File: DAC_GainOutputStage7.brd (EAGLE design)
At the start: 110 x 105.3 mm, 70 parts, among them J1 1935190, J3 SJ-63033A, U1 LM317MQDCYR, U2 LM317MQDCYR

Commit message: Adding trimmer resistor for CCS
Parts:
- removed R10, R16: 48.7, Dual Mono Amp Library:0207/10
- added TP1, TP2: TPB2,54, Dual Mono Amp Library:B2,54
- added VR1, VR2: PVG5A101C03R00, Dual Mono Amp Library:PVG5A101C03R00
- moved R3O 16.0 mm to (2.03, 58.9), turned to 90 degrees
- moved R3O1 16.0 mm to (108.0, 58.9), turned to 90 degrees
- moved U1 11.0 mm to (15.5, 48.5), turned to 270 degrees
- moved U2 11.0 mm to (94.5, 48.5)
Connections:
- net AGND: now also VR1.3, VR2.3; no longer R10.1, R16.1
- net N$23: now also TP1.TP
- net N$29: now also TP2.TP
- net N$37: now also VR2.1, VR2.2; no longer R10.2
- net N$38: now also VR1.1, VR1.2; no longer R16.2
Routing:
- net N$17: track 56.1 -> 73.6 mm, vias 0 -> 1
- net N$16: track 55.4 -> 72.4 mm
- net N$23: track 67.8 -> 82.6 mm
- net N$29: track 52.6 -> 67.4 mm
- net N$22: track 102.9 -> 91.9 mm
- net N$7: track 91.3 -> 83.5 mm
- net N$38: track 11.3 -> 18.1 mm
- net N$37: track 11.3 -> 17.8 mm

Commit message: Ordered boards
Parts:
- added TP3, TP4: TPB2,54, Dual Mono Amp Library:B2,54
- moved TP2 2.23 mm to (108.0, 4.00)
- moved TP1 2.23 mm to (2.03, 4.00)
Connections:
- net N$18: now also TP3.TP
- net N$3: now also TP4.TP
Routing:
- net N$25: track 42.5 -> 53.3 mm
- net 66.3VAC/2: track 284.0 -> 289.9 mm
- net N$3: track 58.8 -> 62.3 mm
- net N$18: track 47.0 -> 50.5 mm
- net N$17: track 73.6 -> 76.5 mm, vias 1 -> 0
- net N$14: track 42.0 -> 43.8 mm
- net N$2: track 43.5 -> 45.3 mm
- net N$22: track 91.9 -> 90.5 mm
- net N$19: track 22.1 -> 23.1 mm
- net N$31: track 22.2 -> 23.2 mm
- net N$34: track 42.6 -> 43.5 mm
- net N$29: track 67.4 -> 68.0 mm
- net N$23: track 82.6 -> 83.2 mm
- net N$13: track 58.0 -> 57.9 mm, vias 1 -> 0
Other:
- board text added: "240"
- board text added: "66.3"
- board text added: "AGND"
- board text added: "LC"
- board text added: "LG"
- board text added: "PE"
- board text added: "RC"
- board text added: "RG"

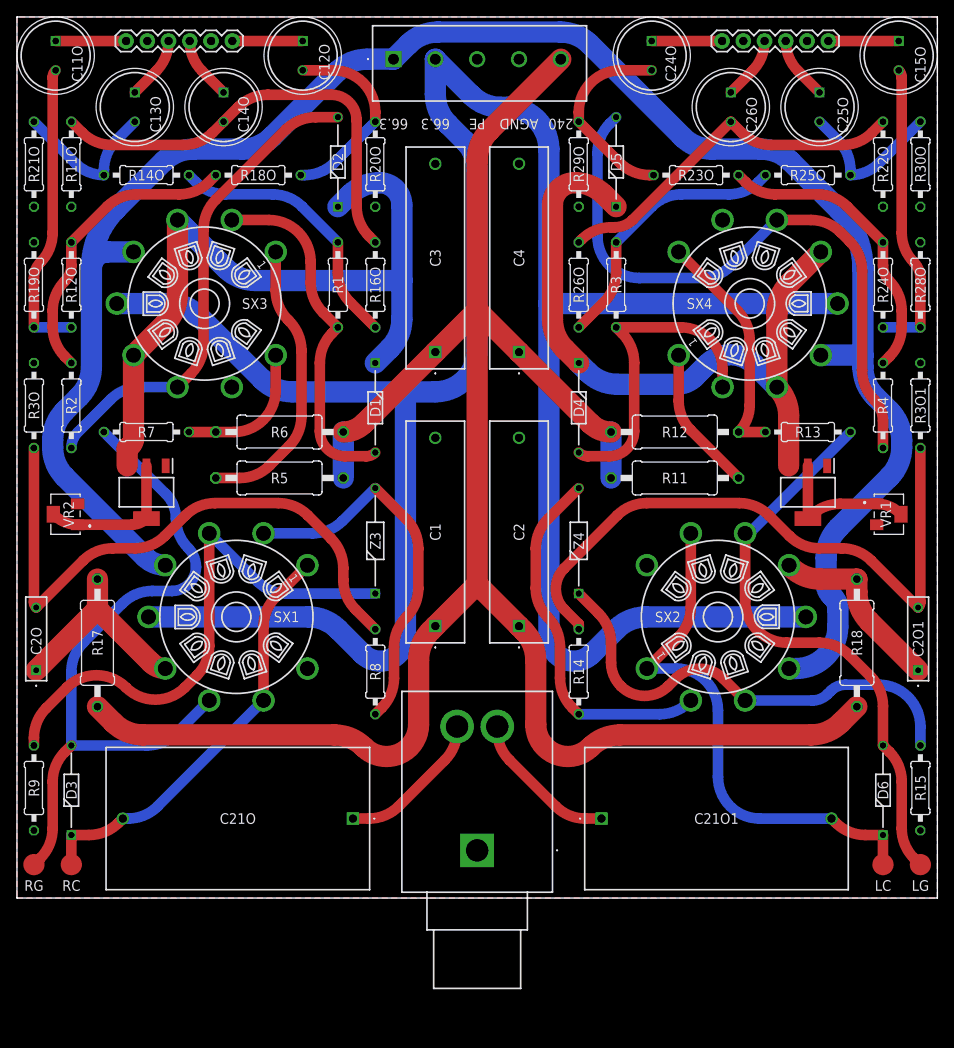
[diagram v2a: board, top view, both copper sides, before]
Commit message: Updated PSU and added headphone protection to output stage
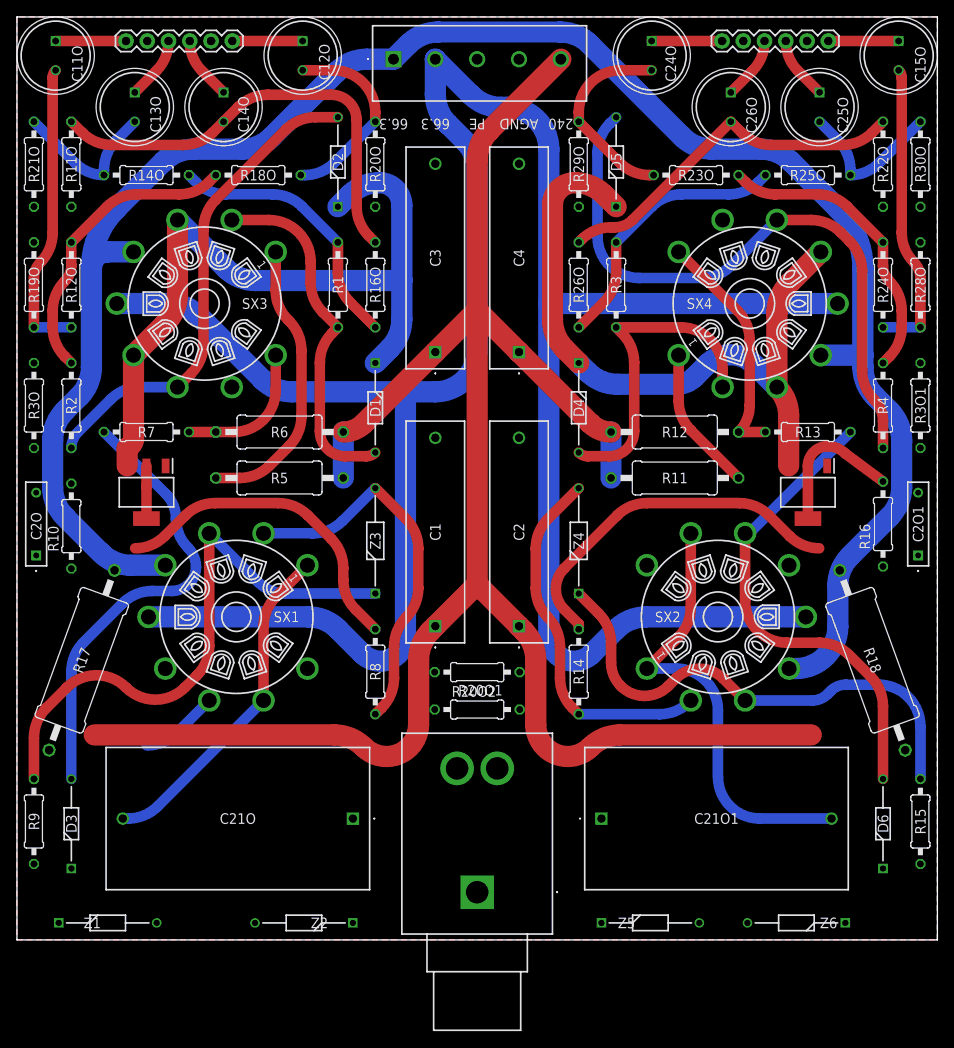
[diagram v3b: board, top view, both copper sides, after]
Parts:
- removed TP1, TP2, TP3, TP4: TPB2,54, Dual Mono Amp Library:B2,54
- removed VR1, VR2: PVG5A101C03R00, Dual Mono Amp Library:PVG5A101C03R00
- added R10, R16: RN55D48R7FB14, Dual Mono Amp Library:0207/10
- added R20O1, R20O2: 10k, Dual Mono Amp Library:0207/10
- added Z1, Z2, Z5, Z6: (no value), Dual Mono Amp Library:DIOAD1165W56L425D185
- R15, R9: value 330 -> 698
- R17, R18: value 499 -> 1k; device Dual Mono Amp Library:0411/15 -> Dual Mono Amp Library:0617/22
- moved C2O 13.7 mm to (2.30, 40.9)
- moved C2O1 13.7 mm to (107.7, 40.9)
- moved J3 5.00 mm to (55.0, 0.70)
- moved R15 4.00 mm to (108.0, 9.16)
- moved R9 4.00 mm to (2.03, 9.16)
- moved D3 4.00 mm to (6.50, 3.54)
- moved D6 4.00 mm to (103.5, 3.54)
- moved R18 2.80 mm to (102.2, 28.4), turned to 290 degrees
- moved R17 2.80 mm to (7.75, 28.4), turned to 70 degrees
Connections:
- new net N$41: Z1.2, Z2.2
- new net N$42: Z5.2, Z6.2
- net AGND: now also R10.1, R16.1, R20O1.1, R20O2.1, Z1.1, Z6.1; no longer VR1.3, VR2.3
- net L_OUT: now also R20O2.2, Z5.1
- net N$18: no longer TP3.TP
- net N$23: no longer TP1.TP
- net N$29: no longer TP2.TP
- net N$3: no longer TP4.TP
- net N$37: now also R10.2; no longer VR2.1, VR2.2
- net N$38: now also R16.2; no longer VR1.1, VR1.2
- net R_OUT: now also R20O1.2, Z2.1
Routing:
- net N$17: track 76.5 -> 43.0 mm
- net N$16: track 72.4 -> 38.8 mm
- net N$39: track 24.8 -> 0.00 mm
- net N$40: track 22.1 -> 0.00 mm
- net N$23: track 83.2 -> 62.7 mm
- net R_OUT: track 17.9 -> 0.00 mm
- net L_OUT: track 17.9 -> 0.00 mm
- net N$37: track 17.8 -> 6.30 mm
- net N$29: track 68.0 -> 56.6 mm
- net N$3: track 62.3 -> 52.2 mm
- net N$18: track 50.5 -> 40.4 mm
- net +240VDC: track 240.4 -> 233.2 mm
- net N$27: track 54.6 -> 58.6 mm
- net N$26: track 64.2 -> 68.2 mm
- net 66.3VAC/1: track 226.0 -> 227.8 mm
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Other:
- board size 110 x 105.3 mm -> 110 x 110.3 mm
- board text removed: "LC"
- board text removed: "LG"
- board text removed: "RC"
- board text removed: "RG"
